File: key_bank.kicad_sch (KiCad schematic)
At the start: 20 parts, among them IC2 ADG726BSUZ

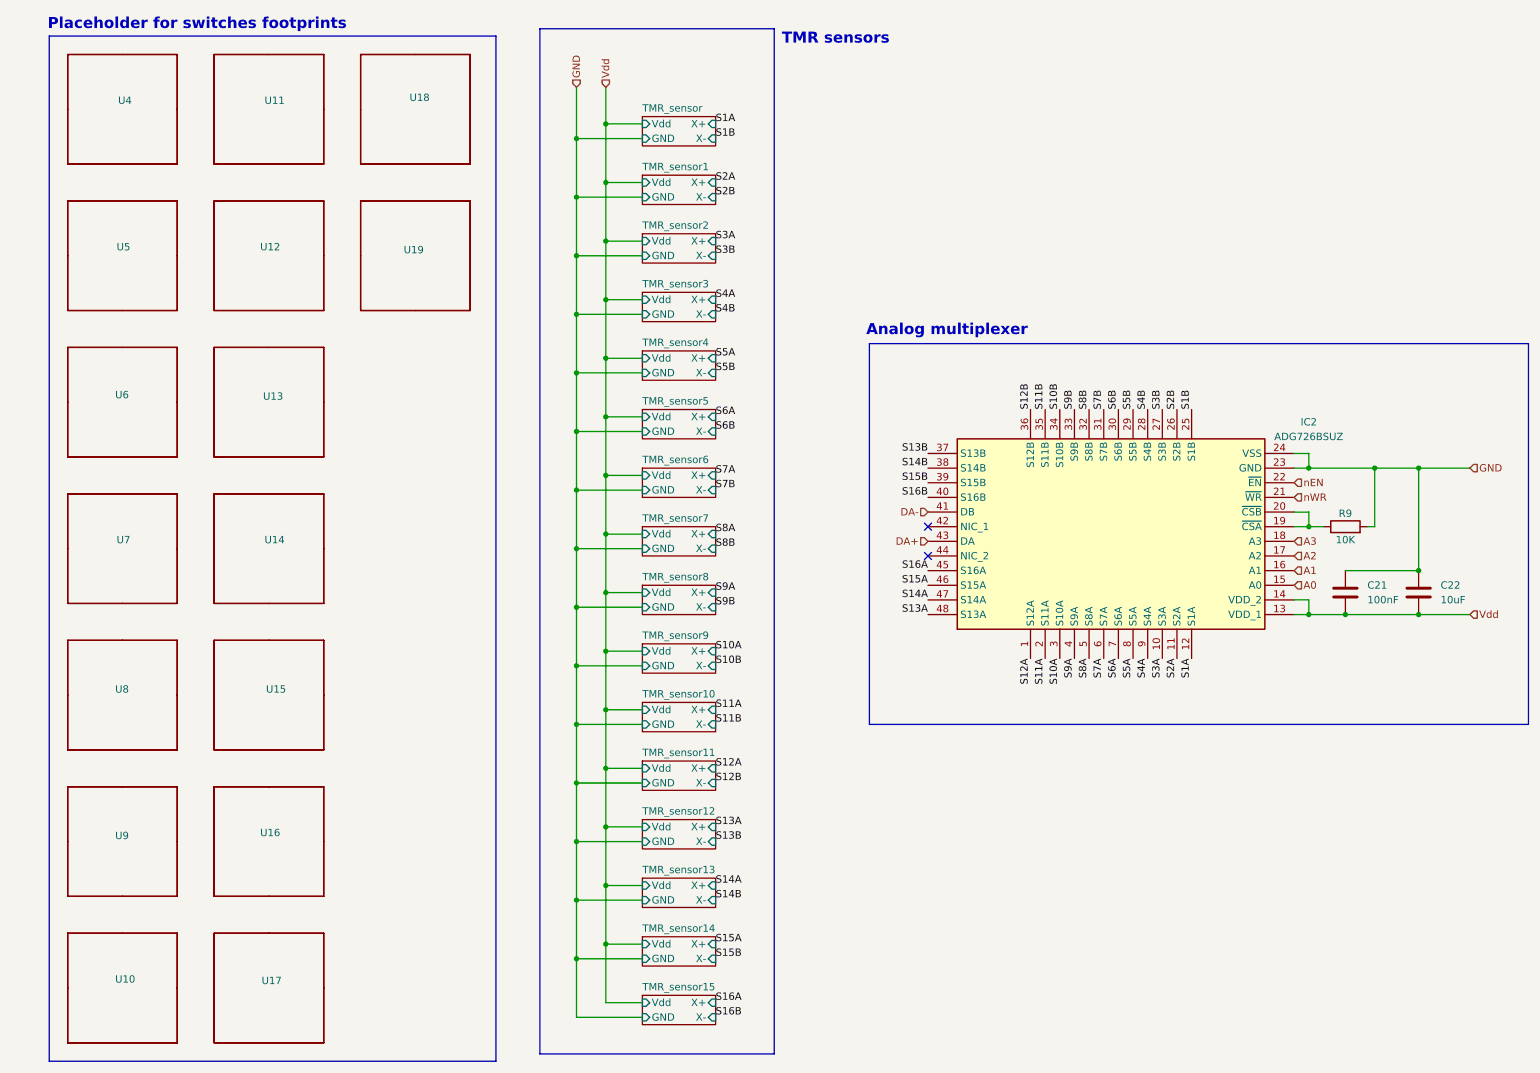
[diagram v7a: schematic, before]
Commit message: [FIX](USB) main usb net labels
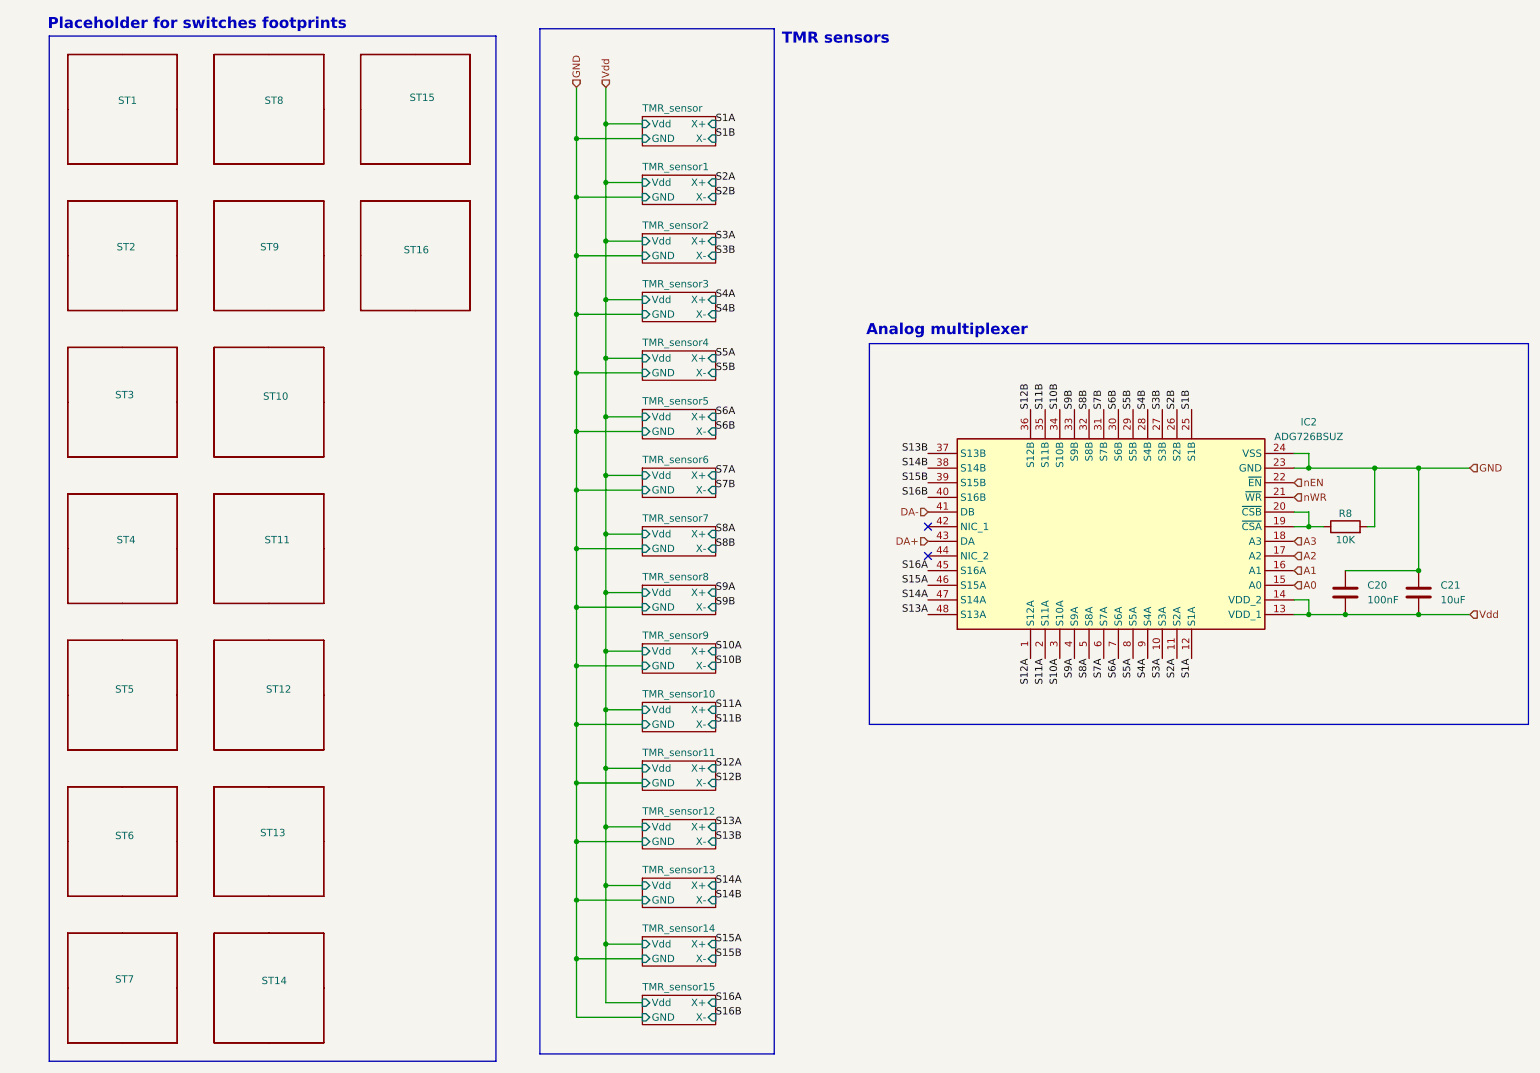
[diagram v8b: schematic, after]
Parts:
- renumbered C21 to C20, C22 to C21, R9 to R8, U4 to ST1, U13 to ST10, U14 to ST11, U15 to ST12, U16 to ST13, U17 to ST14, U18 to ST15, U19 to ST16, U5 to ST2, U6 to ST3, U7 to ST4, U8 to ST5, U9 to ST6, U10 to ST7, U11 to ST8, U12 to ST9
